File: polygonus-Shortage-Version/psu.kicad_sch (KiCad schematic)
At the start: 36 parts, among them U1004 TLS115, U1005 TLS115, U11 MCP2551-I-SN, U6 MCP2551-I-SN, U902 AMS1117-3.3, U903 LMR14020

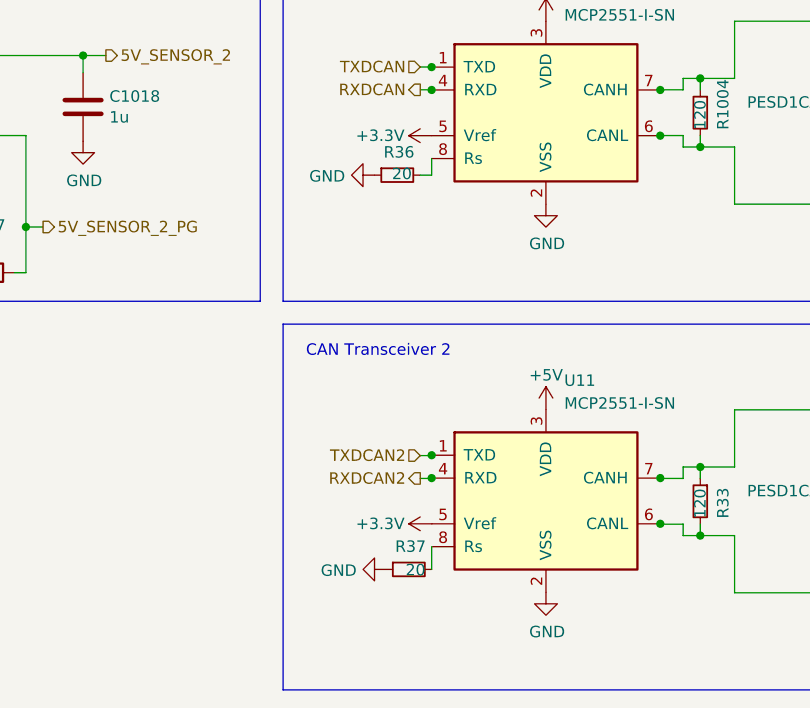
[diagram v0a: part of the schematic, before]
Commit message: Added Hall input stuff for VR pins
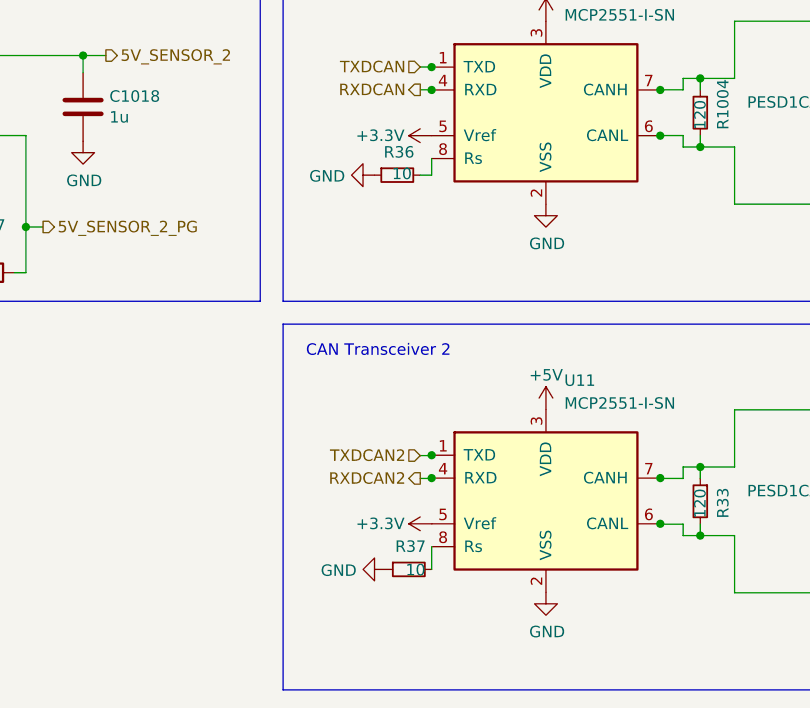
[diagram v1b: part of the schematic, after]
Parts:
- R36, R37: value 20 -> 10
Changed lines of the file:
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@@
       (effects (font (size 1.27 1.27)) (justify left))
     )
-    (property "Value" "20" (id 1) (at 175.6038 88.7091 90)
+    (property "Value" "10" (id 1) (at 175.6038 88.7091 90)
       (effects (font (size 1.27 1.27)) (justify left))
     )
@@
       (effects (font (size 1.27 1.27)) (justify left))
     )
-    (property "Value" "20" (id 1) (at 177.113 132.7277 90)
+    (property "Value" "10" (id 1) (at 177.113 132.7277 90)
       (effects (font (size 1.27 1.27)) (justify left))
     )

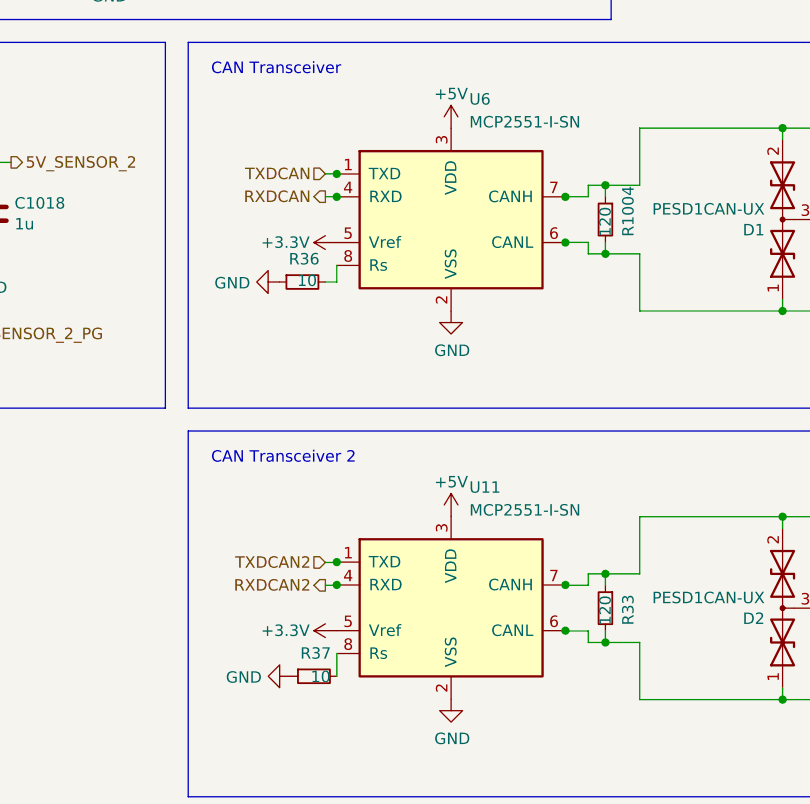
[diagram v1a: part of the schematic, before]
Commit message: DRC completed
LS gives errors due to only tab connected, deliberate.
Some silk screen overlaps.
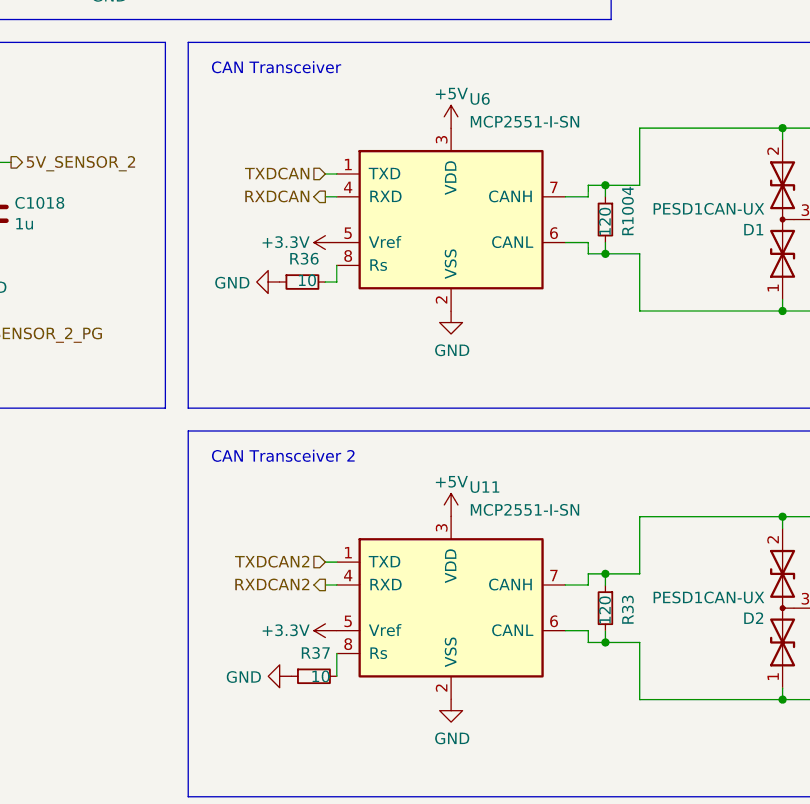
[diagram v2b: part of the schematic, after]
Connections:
- net CANH: now also U6.7 (CANH)
- net CANH2: now also U11.7 (CANH)
- net CANL: now also U6.6 (CANL)
- net CANL2: now also U11.6 (CANL)
- net RXDCAN: now also U6.4 (RXD)
- net RXDCAN2: now also U11.4 (RXD)
- net TXDCAN: now also U6.1 (TXD)
- net TXDCAN2: now also U11.1 (TXD)
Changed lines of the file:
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@@
   (junction (at 36.195 29.21) (diameter 0) (color 0 0 0 0)
   )
-  (junction (at 203.1939 79.3912) (diameter 0) (color 0 0 0 0)
-  )
   (junction (at 108.585 29.21) (diameter 0) (color 0 0 0 0)
   )
@@
   (junction (at 207.645 78.105) (diameter 0) (color 0 0 0 0)
   )
-  (junction (at 177.7939 79.3912) (diameter 0) (color 0 0 0 0)
-  )
   (junction (at 20.32 75.565) (diameter 0) (color 0 0 0 0)
   )
-  (junction (at 203.1992 127.596) (diameter 0) (color 0 0 0 0)
-  )
   (junction (at 227.33 114.935) (diameter 0) (color 0 0 0 0)
   )
@@
   (junction (at 99.695 29.21) (diameter 0) (color 0 0 0 0)
   )
-  (junction (at 177.7992 119.976) (diameter 0) (color 0 0 0 0)
-  )
-  (junction (at 177.7992 122.516) (diameter 0) (color 0 0 0 0)
-  )
   (junction (at 207.645 85.725) (diameter 0) (color 0 0 0 0)
   )
@@
   (junction (at 154.94 41.91) (diameter 0) (color 0 0 0 0)
   )
-  (junction (at 203.1939 84.4712) (diameter 0) (color 0 0 0 0)
-  )
-  (junction (at 203.1992 122.516) (diameter 0) (color 0 0 0 0)
-  )
   (junction (at 227.33 135.255) (diameter 0) (color 0 0 0 0)
   )
-  (junction (at 177.7939 76.8512) (diameter 0) (color 0 0 0 0)
-  )
   (junction (at 31.75 29.21) (diameter 0) (color 0 0 0 0)
   )
-  (wire (pts (xy 205.74 127.635) (xy 205.74 128.905))
+  (wire (pts (xy 205.7392 127.596) (xy 205.74 128.905))
     (stroke (width 0) (type default) (color 0 0 0 0))
   )
@@
     (stroke (width 0) (type default) (color 0 0 0 0))
   )
-  (wire (pts (xy 176.53 122.555) (xy 177.8 122.555))
+  (wire (pts (xy 176.5292 122.516) (xy 177.7992 122.516))
     (stroke (width 0) (type default) (color 0 0 0 0))
   )
@@
     (stroke (width 0) (type default) (color 0 0 0 0))
   )
-  (wire (pts (xy 205.74 79.375) (xy 205.74 78.105))
+  (wire (pts (xy 205.7339 79.3912) (xy 205.74 78.105))
     (stroke (width 0) (type default) (color 0 0 0 0))
   )
@@
     (stroke (width 0) (type default) (color 0 0 0 0))
   )
-  (wire (pts (xy 203.2 122.555) (xy 205.74 122.555))
+  (wire (pts (xy 203.1992 122.516) (xy 205.7392 122.516))
     (stroke (width 0) (type default) (color 0 0 0 0))
   )
@@
     (stroke (width 0) (type default) (color 0 0 0 0))
   )
-  (wire (pts (xy 177.8 120.015) (xy 176.53 120.015))
+  (wire (pts (xy 177.7992 119.976) (xy 176.5292 119.976))
     (stroke (width 0) (type default) (color 0 0 0 0))
   )
@@
     (stroke (width 0) (type default) (color 0 0 0 0))
   )
-  (wire (pts (xy 177.8 76.835) (xy 176.53 76.835))
-    (stroke (width 0) (type default) (color 0 0 0 0))
-  )
-  (wire (pts (xy 176.53 79.375) (xy 177.8 79.375))
+  (wire (pts (xy 177.7939 76.8512) (xy 176.5239 76.8512))
+    (stroke (width 0) (type default) (color 0 0 0 0))
+  )
+  (wire (pts (xy 176.5239 79.3912) (xy 177.7939 79.3912))
     (stroke (width 0) (type default) (color 0 0 0 0))
   )
@@
     (stroke (width 0) (type default) (color 0 0 0 0))
   )
-  (wire (pts (xy 203.2 84.455) (xy 205.74 84.455))
+  (wire (pts (xy 203.1939 84.4712) (xy 205.7339 84.4712))
     (stroke (width 0) (type default) (color 0 0 0 0))
   )
@@
     (stroke (width 0) (type default) (color 0 0 0 0))
   )
-  (wire (pts (xy 205.74 84.455) (xy 205.74 85.725))
+  (wire (pts (xy 205.7339 84.4712) (xy 205.74 85.725))
     (stroke (width 0) (type default) (color 0 0 0 0))
   )
@@
     (stroke (width 0) (type default) (color 0 0 0 0))
   )
-  (wire (pts (xy 205.74 122.555) (xy 205.74 121.285))
+  (wire (pts (xy 205.7392 122.516) (xy 205.74 121.285))
     (stroke (width 0) (type default) (color 0 0 0 0))
   )
@@
     (stroke (width 0) (type default) (color 0 0 0 0))
   )
-  (wire (pts (xy 203.2 79.375) (xy 205.74 79.375))
+  (wire (pts (xy 203.1939 79.3912) (xy 205.7339 79.3912))
     (stroke (width 0) (type default) (color 0 0 0 0))
   )
@@
     (stroke (width 0) (type default) (color 0 0 0 0))
   )
-  (wire (pts (xy 203.2 127.635) (xy 205.74 127.635))
+  (wire (pts (xy 203.1992 127.596) (xy 205.7392 127.596))
     (stroke (width 0) (type default) (color 0 0 0 0))
   )
@@
     (effects (font (size 1.27 1.27)) (justify left bottom))
   )
-  (hierarchical_label "RXDCAN" (shape output) (at 176.53 79.375 180)
+  (hierarchical_label "RXDCAN" (shape output) (at 176.5239 79.3912 180)
     (effects (font (size 1.27 1.27)) (justify right))
   )
@@
     (effects (font (size 1.27 1.27)) (justify right))
   )
-  (hierarchical_label "TXDCAN2" (shape input) (at 176.53 120.015 180)
+  (hierarchical_label "TXDCAN2" (shape input) (at 176.5292 119.976 180)
     (effects (font (size 1.27 1.27)) (justify right))
   )
@@
     (effects (font (size 1.27 1.27)) (justify left))
   )
-  (hierarchical_label "TXDCAN" (shape input) (at 176.53 76.835 180)
+  (hierarchical_label "TXDCAN" (shape input) (at 176.5239 76.8512 180)
     (effects (font (size 1.27 1.27)) (justify right))
   )
@@
     (effects (font (size 1.27 1.27)) (justify left))
   )
-  (hierarchical_label "RXDCAN2" (shape output) (at 176.53 122.555 180)
+  (hierarchical_label "RXDCAN2" (shape output) (at 176.5292 122.516 180)
     (effects (font (size 1.27 1.27)) (justify right))
   )

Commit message: clearout basic version
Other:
- company: rusEFI -> (none)
- title: rusEfi Proteus -> Polygonus
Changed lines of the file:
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@@
   (paper "A4")
   (title_block
-    (title "rusEfi Proteus")
-    (date "2022-04-09")
+    (title "Polygonus")
+    (date "2023-03-15")
     (rev "v0.7")
-    (company "rusEFI")
-    (comment 1 "github.com/mck1117/proteus")
     (comment 2 "rusefi.com/s/proteus")
   )

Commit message: Update to V1.3
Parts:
- renumbered C904 to C10, C905 to C11, C1004 to C12, C906 to C13, C903 to C14, C1015 to C2, C1016 to C3, C1006 to C4, C1017 to C5, C1001 to C6, C1002 to C7, C902 to C8, C1018 to C9, D1001 to D1, D903 to D2, D901 to D3, D1 to D4, D2 to D5, L1002 to L1, L1001 to L2, R1006 to R1, R33 to R10, R906 to R2, R905 to R3, R1007 to R4, R907 to R5, R908 to R6, R36 to R7, R37 to R8, R1004 to R9, U1004 to U1, U1005 to U2, U903 to U3, U6 to U4, U11 to U5, U902 to U6
